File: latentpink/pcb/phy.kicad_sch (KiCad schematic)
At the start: 173 parts, among them J1 CONN_SFP_HOST, J18 BEL_FUSE_0845-2R1T-E4, J19 BEL_FUSE_0845-2R1T-E4, J2 SFP_CAGE, J20 BEL_FUSE_0845-2R1T-E4, J21 BEL_FUSE_0845-2R1T-E4, J3 XILINX_JTAG, J4 BEL_FUSE_0845-2R1T-E4, J8 BEL_FUSE_0845-2R1T-E4, M1 960-27-12-D-AB-0, U1 VSC8512, U2 XC7K160T-2FBG484C, U24 SIT9121AI-2BF-XXS200.000000G, U25 SIT9121AI-2BF-XXS156.250000G, U31 74LVC1T45, U32 74LVC1T45, U33 74LVC1T45, U34 74LVC1T45, U35 SIT9121AC-2B2-33E125.000000, U4 STM32H735-UFBGA176-25, U40 RCLAMP0514M, U41 RCLAMP0514M, U42 RCLAMP0514M, U43 RCLAMP0514M, U44 RCLAMP0514M, U45 RCLAMP0514M, U46 RCLAMP0514M, U47 RCLAMP0514M, U48 RCLAMP0514M, U49 RCLAMP0514M, U50 RCLAMP0514M, U51 RCLAMP0514M, U52 RCLAMP0514M, U53 RCLAMP0514M, U54 RCLAMP0514M, U55 RCLAMP0514M, U56 RCLAMP0514M, U57 RCLAMP0514M, U58 RCLAMP0514M, U59 RCLAMP0514M, U60 RCLAMP0514M, U61 RCLAMP0514M, U62 RCLAMP0514M, U63 RCLAMP0514M

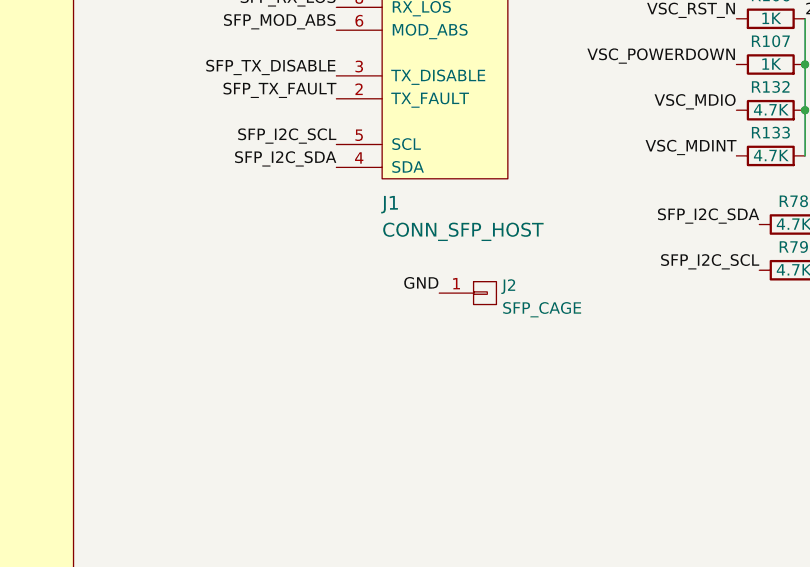
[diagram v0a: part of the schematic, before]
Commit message: Progress on management / power region at south
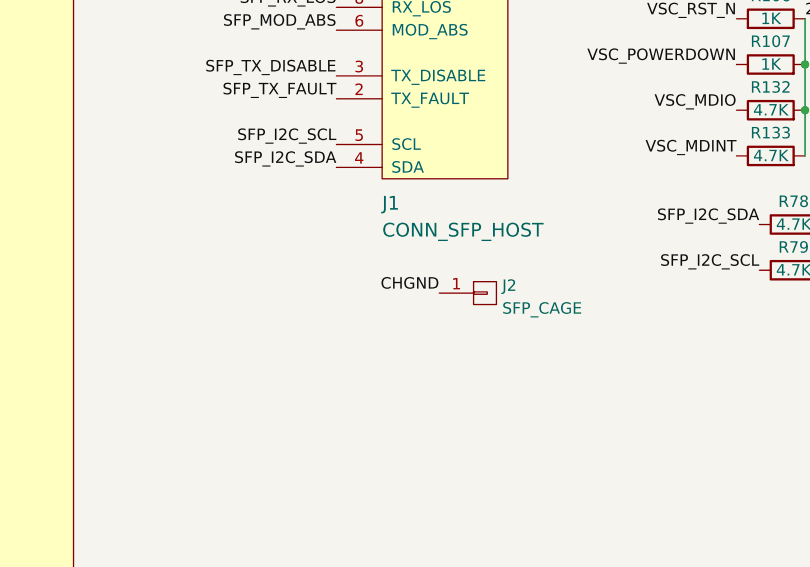
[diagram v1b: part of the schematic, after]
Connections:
- net CHGND: now also J2.1 (P1)
- net GND: no longer J2.1 (P1)
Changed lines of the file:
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@@
     (effects (font (size 1.27 1.27)) (justify right bottom))
   )
-  (label "GND" (at 133.35 284.48 180)
+  (label "CHGND" (at 133.35 284.48 180)
     (effects (font (size 1.27 1.27)) (justify right bottom))
   )

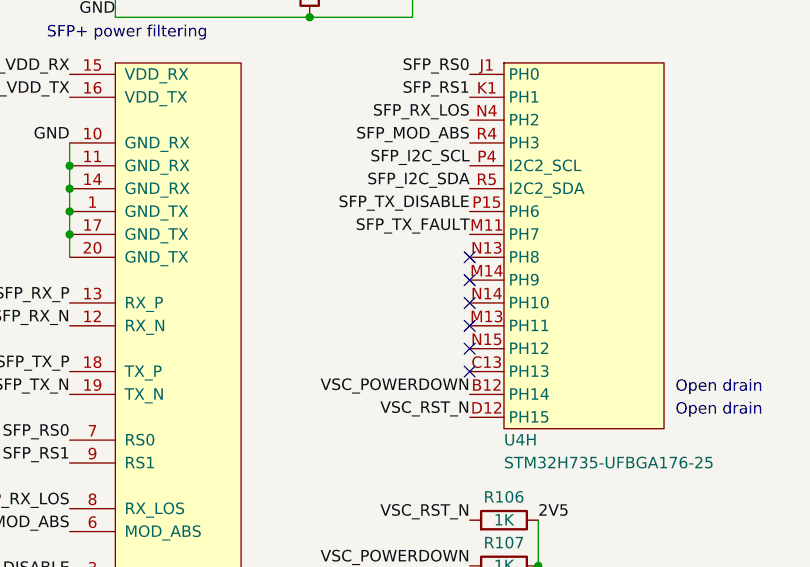
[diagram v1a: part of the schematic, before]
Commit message: Continued work on management MCU area
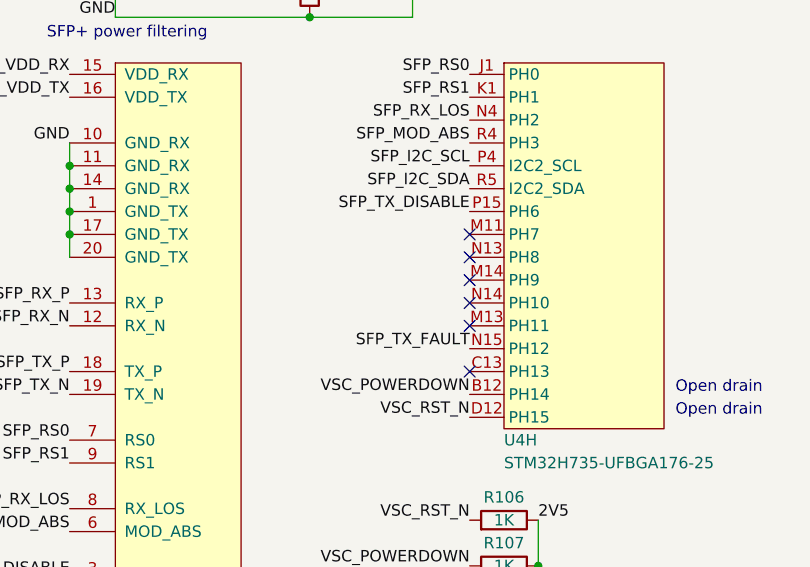
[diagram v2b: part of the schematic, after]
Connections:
- net SFP_TX_FAULT: now also U4.N15 (PH12); no longer U4.M11 (PH7)
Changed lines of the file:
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@@
   (no_connect (at 50.8 147.32))
   (no_connect (at 166.37 237.49))
-  (no_connect (at 166.37 234.95))
   (no_connect (at 173.99 365.76))
   (no_connect (at 97.79 154.94))
@@
   (no_connect (at 166.37 229.87))
   (no_connect (at 50.8 104.14))
+  (no_connect (at 166.37 222.25))
   (no_connect (at 50.8 185.42))
   (no_connect (at 97.79 144.78))
@@
     (effects (font (size 1.27 1.27)) (justify right bottom))
   )
-  (label "SFP_TX_FAULT" (at 166.37 222.25 180)
-    (effects (font (size 1.27 1.27)) (justify right bottom))
-  )
+  (label "SFP_TX_FAULT" (at 166.37 234.95 180)
+    (effects (font (size 1.27 1.27)) (justify right bottom))
+  )

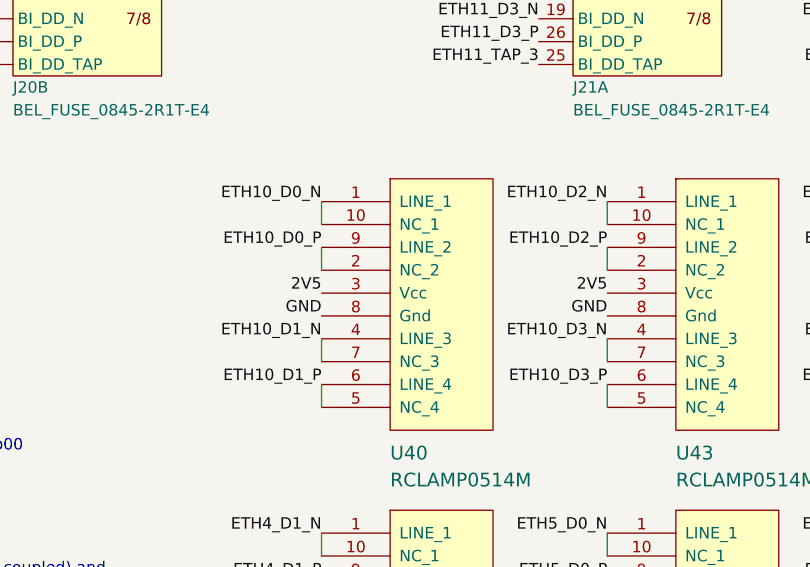
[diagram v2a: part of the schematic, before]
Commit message: Routed upper SGMII PHY except for bus to FPGA
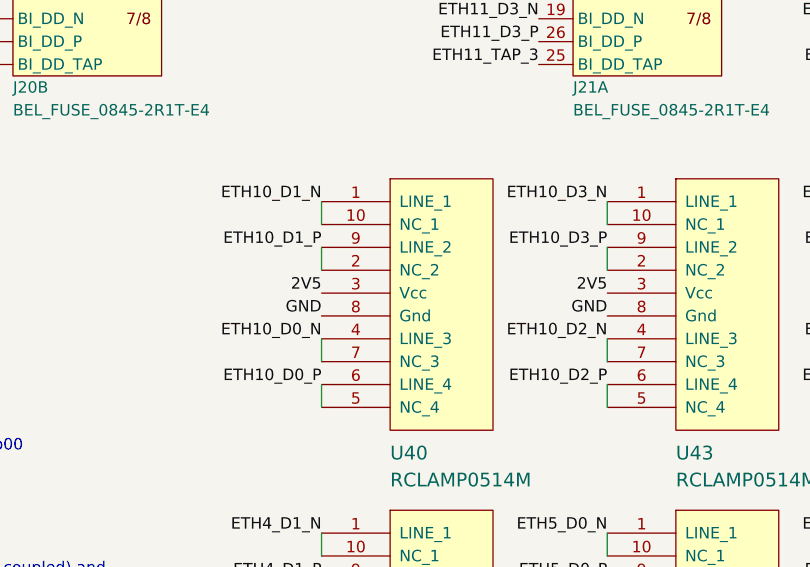
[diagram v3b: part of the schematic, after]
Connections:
- net ETH10_D0_N: now also U40.4 (LINE_3), U40.7 (NC_3); no longer U40.1 (LINE_1), U40.10 (NC_1)
- net ETH10_D0_P: now also U40.5 (NC_4), U40.6 (LINE_4); no longer U40.2 (NC_2), U40.9 (LINE_2)
- net ETH10_D1_N: now also U40.1 (LINE_1), U40.10 (NC_1); no longer U40.4 (LINE_3), U40.7 (NC_3)
- net ETH10_D1_P: now also U40.2 (NC_2), U40.9 (LINE_2); no longer U40.5 (NC_4), U40.6 (LINE_4)
- net ETH10_D2_N: now also U43.4 (LINE_3), U43.7 (NC_3); no longer U43.1 (LINE_1), U43.10 (NC_1)
- net ETH10_D2_P: now also U43.5 (NC_4), U43.6 (LINE_4); no longer U43.2 (NC_2), U43.9 (LINE_2)
- net ETH10_D3_N: now also U43.1 (LINE_1), U43.10 (NC_1); no longer U43.4 (LINE_3), U43.7 (NC_3)
- net ETH10_D3_P: now also U43.2 (NC_2), U43.9 (LINE_2); no longer U43.5 (NC_4), U43.6 (LINE_4)
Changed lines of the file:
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@@
   (paper "A2")
   (title_block
-    (date "2023-05-27")
+    (date "2023-05-28")
     (rev "0.1")
     (company "Antikernel Labs")
@@
     (effects (font (size 1.27 1.27)) (justify right bottom))
   )
-  (label "ETH10_D2_P" (at 429.26 227.33 180)
+  (label "ETH10_D2_P" (at 429.26 242.57 180)
     (effects (font (size 1.27 1.27)) (justify right bottom))
   )
@@
     (effects (font (size 1.27 1.27)) (justify right bottom))
   )
-  (label "ETH10_D1_N" (at 397.51 237.49 180)
+  (label "ETH10_D1_N" (at 397.51 222.25 180)
     (effects (font (size 1.27 1.27)) (justify right bottom))
   )
@@
     (effects (font (size 1.27 1.27)) (justify right bottom))
   )
-  (label "ETH10_D2_N" (at 429.26 222.25 180)
+  (label "ETH10_D2_N" (at 429.26 237.49 180)
     (effects (font (size 1.27 1.27)) (justify right bottom))
   )
@@
     (effects (font (size 1.27 1.27)) (justify left bottom))
   )
-  (label "ETH10_D3_P" (at 429.26 242.57 180)
+  (label "ETH10_D3_P" (at 429.26 227.33 180)
     (effects (font (size 1.27 1.27)) (justify right bottom))
   )
@@
     (effects (font (size 1.27 1.27)) (justify right bottom))
   )
-  (label "ETH10_D0_N" (at 397.51 222.25 180)
+  (label "ETH10_D0_N" (at 397.51 237.49 180)
     (effects (font (size 1.27 1.27)) (justify right bottom))
   )
@@
     (effects (font (size 1.27 1.27)) (justify left bottom))
   )
-  (label "ETH10_D3_N" (at 429.26 237.49 180)
-    (effects (font (size 1.27 1.27)) (justify right bottom))
-  )
-  (label "ETH10_D0_P" (at 397.51 227.33 180)
+  (label "ETH10_D3_N" (at 429.26 222.25 180)
+    (effects (font (size 1.27 1.27)) (justify right bottom))
+  )
+  (label "ETH10_D0_P" (at 397.51 242.57 180)
     (effects (font (size 1.27 1.27)) (justify right bottom))
   )
@@
     (effects (font (size 1.27 1.27)) (justify right bottom))
   )
-  (label "ETH10_D1_P" (at 397.51 242.57 180)
-    (effects (font (size 1.27 1.27)) (justify right bottom))
-  )
+  (label "ETH10_D1_P" (at 397.51 227.33 180)
+    (effects (font (size 1.27 1.27)) (justify right bottom))
+  )

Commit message: Began QDR layout
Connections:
- net QSGMII_2_RX_AC_N: now also U1.Y9 (SERDES_E3_TX_P); no longer U1.AA9 (SERDES_E3_TX_N)
- net QSGMII_2_RX_AC_P: now also U1.AA9 (SERDES_E3_TX_N); no longer U1.Y9 (SERDES_E3_TX_P)
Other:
- note added: "Polarity swap Invert in FPGA"
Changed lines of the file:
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@@
     (stroke (width 0) (type default) (color 0 0 0 0))
+  )
+  (text "Polarity swap\nInvert in FPGA" (at 119.38 127 0)
+    (effects (font (size 1.27 1.27)) (justify left bottom))
   )
   (text "Refclk is LVDS (must be AC coupled) and\ninternally terminated / biased\n(Fig. 12 on page 16)"
@@
     (effects (font (size 1.27 1.27)) (justify left bottom))
   )
-  (label "QSGMII_2_RX_AC_N" (at 99.06 124.46 0)
+  (label "QSGMII_2_RX_AC_N" (at 99.06 127 0)
     (effects (font (size 1.27 1.27)) (justify left bottom))
   )
@@
     (effects (font (size 1.27 1.27)) (justify left bottom))
   )
-  (label "QSGMII_2_RX_AC_P" (at 99.06 127 0)
-    (effects (font (size 1.27 1.27)) (justify left bottom))
-  )
+  (label "QSGMII_2_RX_AC_P" (at 99.06 124.46 0)
+    (effects (font (size 1.27 1.27)) (justify left bottom))
+  )

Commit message: Lots more layout of low speed stuff and power. Partial layout of 1.2V supply. Initial RGMII escape routing.
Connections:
- net SFP_RX_N: now also U2.B6 (GTX_RX_3_P); no longer U2.B5 (GTX_RX_3_N)
- net SFP_RX_P: now also U2.B5 (GTX_RX_3_N); no longer U2.B6 (GTX_RX_3_P)
- net SFP_TX_N: now also U2.A4 (GTX_TX_3_P); no longer U2.A3 (GTX_TX_3_N)
- net SFP_TX_P: now also U2.A3 (GTX_TX_3_N); no longer U2.A4 (GTX_TX_3_P)
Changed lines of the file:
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@@
   (paper "A2")
   (title_block
-    (date "2023-05-31")
+    (date "2023-06-01")
     (rev "0.1")
     (company "Antikernel Labs")
@@
     (stroke (width 0) (type default) (color 0 0 0 0))
   )
-  (text "Polarity swap\nInvert in FPGA" (at 119.38 127 0)
+  (text "Polarity swap\nInvert in FPGA" (at 20.32 260.35 0)
     (effects (font (size 1.27 1.27)) (justify left bottom))
   )
@@
     (effects (font (size 5 5) (thickness 0.5) bold) (justify left bottom))
   )
+  (text "Polarity swap\nInvert in FPGA" (at 20.32 207.01 0)
+    (effects (font (size 1.27 1.27)) (justify left bottom))
+  )
   (text "One LED per RJ45 (bi color) but VSC8512 has two single LED pins"
     (at 55.88 86.36 0)
@@
     (effects (font (size 1.27 1.27)) (justify left bottom))
   )
+  (text "Polarity swap\nInvert in FPGA" (at 20.32 214.63 0)
+    (effects (font (size 1.27 1.27)) (justify left bottom))
+  )
   (label "2V5" (at 397.51 269.24 180)
     (effects (font (size 1.27 1.27)) (justify right bottom))
@@
     (effects (font (size 1.27 1.27)) (justify right bottom))
   )
-  (label "SFP_RX_N" (at 50.8 214.63 180)
+  (label "SFP_RX_N" (at 50.8 212.09 180)
     (effects (font (size 1.27 1.27)) (justify right bottom))
   )
@@
     (effects (font (size 1.27 1.27)) (justify right bottom))
   )
-  (label "SFP_RX_P" (at 50.8 212.09 180)
+  (label "SFP_RX_P" (at 50.8 214.63 180)
     (effects (font (size 1.27 1.27)) (justify right bottom))
   )
@@
     (effects (font (size 1.27 1.27)) (justify right bottom))
   )
-  (label "SFP_TX_N" (at 50.8 207.01 180)
+  (label "SFP_TX_N" (at 50.8 204.47 180)
     (effects (font (size 1.27 1.27)) (justify right bottom))
   )
@@
     (effects (font (size 1.27 1.27)) (justify right bottom))
   )
-  (label "SFP_TX_P" (at 50.8 204.47 180)
-    (effects (font (size 1.27 1.27)) (justify right bottom))
-  )
+  (label "SFP_TX_P" (at 50.8 207.01 180)
+    (effects (font (size 1.27 1.27)) (justify right bottom))
+  )

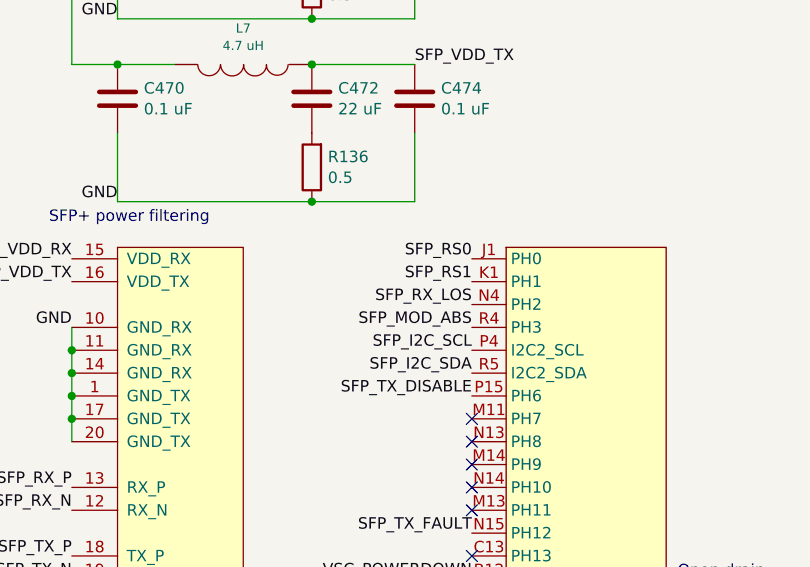
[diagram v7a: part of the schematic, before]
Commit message: Good progress routing QDR with new pinout
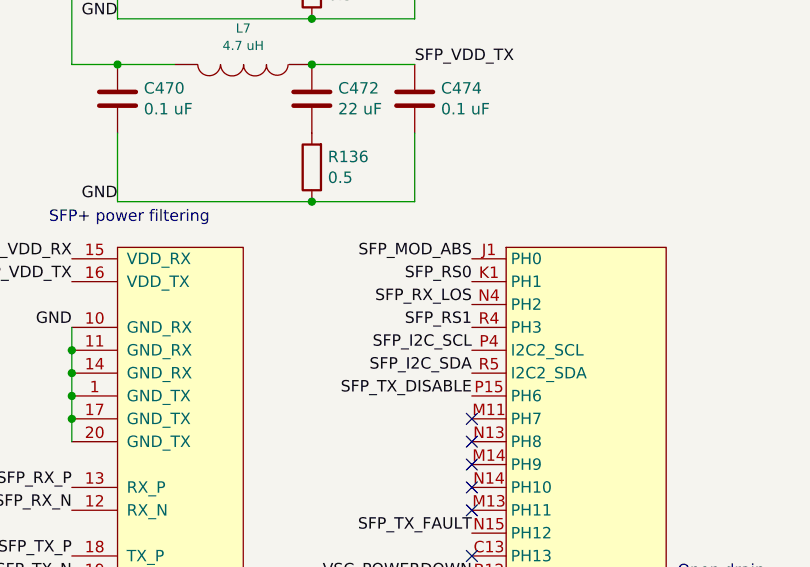
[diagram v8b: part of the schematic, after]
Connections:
- net SFP_MOD_ABS: now also U4.J1 (PH0); no longer U4.R4 (PH3)
- net SFP_RS0: now also U4.K1 (PH1); no longer U4.J1 (PH0)
- net SFP_RS1: now also U4.R4 (PH3); no longer U4.K1 (PH1)
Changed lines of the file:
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@@
     (effects (font (size 1.27 1.27)) (justify right bottom))
   )
-  (label "SFP_RS1" (at 166.37 207.01 180)
+  (label "SFP_RS1" (at 166.37 212.09 180)
     (effects (font (size 1.27 1.27)) (justify right bottom))
   )
@@
     (effects (font (size 1.27 1.27)) (justify left bottom))
   )
-  (label "SFP_MOD_ABS" (at 166.37 212.09 180)
+  (label "SFP_MOD_ABS" (at 166.37 204.47 180)
     (effects (font (size 1.27 1.27)) (justify right bottom))
   )
@@
     (effects (font (size 1.27 1.27)) (justify right bottom))
   )
-  (label "SFP_RS0" (at 166.37 204.47 180)
+  (label "SFP_RS0" (at 166.37 207.01 180)
     (effects (font (size 1.27 1.27)) (justify right bottom))
   )
